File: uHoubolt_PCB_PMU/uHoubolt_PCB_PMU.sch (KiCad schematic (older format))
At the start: 44 parts, among them J1 Conn_01x04, J2 Conn_01x02, J3 Conn_01x04, Q1 ZXMN3F30FH, Q2 Si7141DP, SW1 SW_Push_SPDT, SW2 SW_Push_SPDT, U1 INA226, U2 MAX1873SEEE

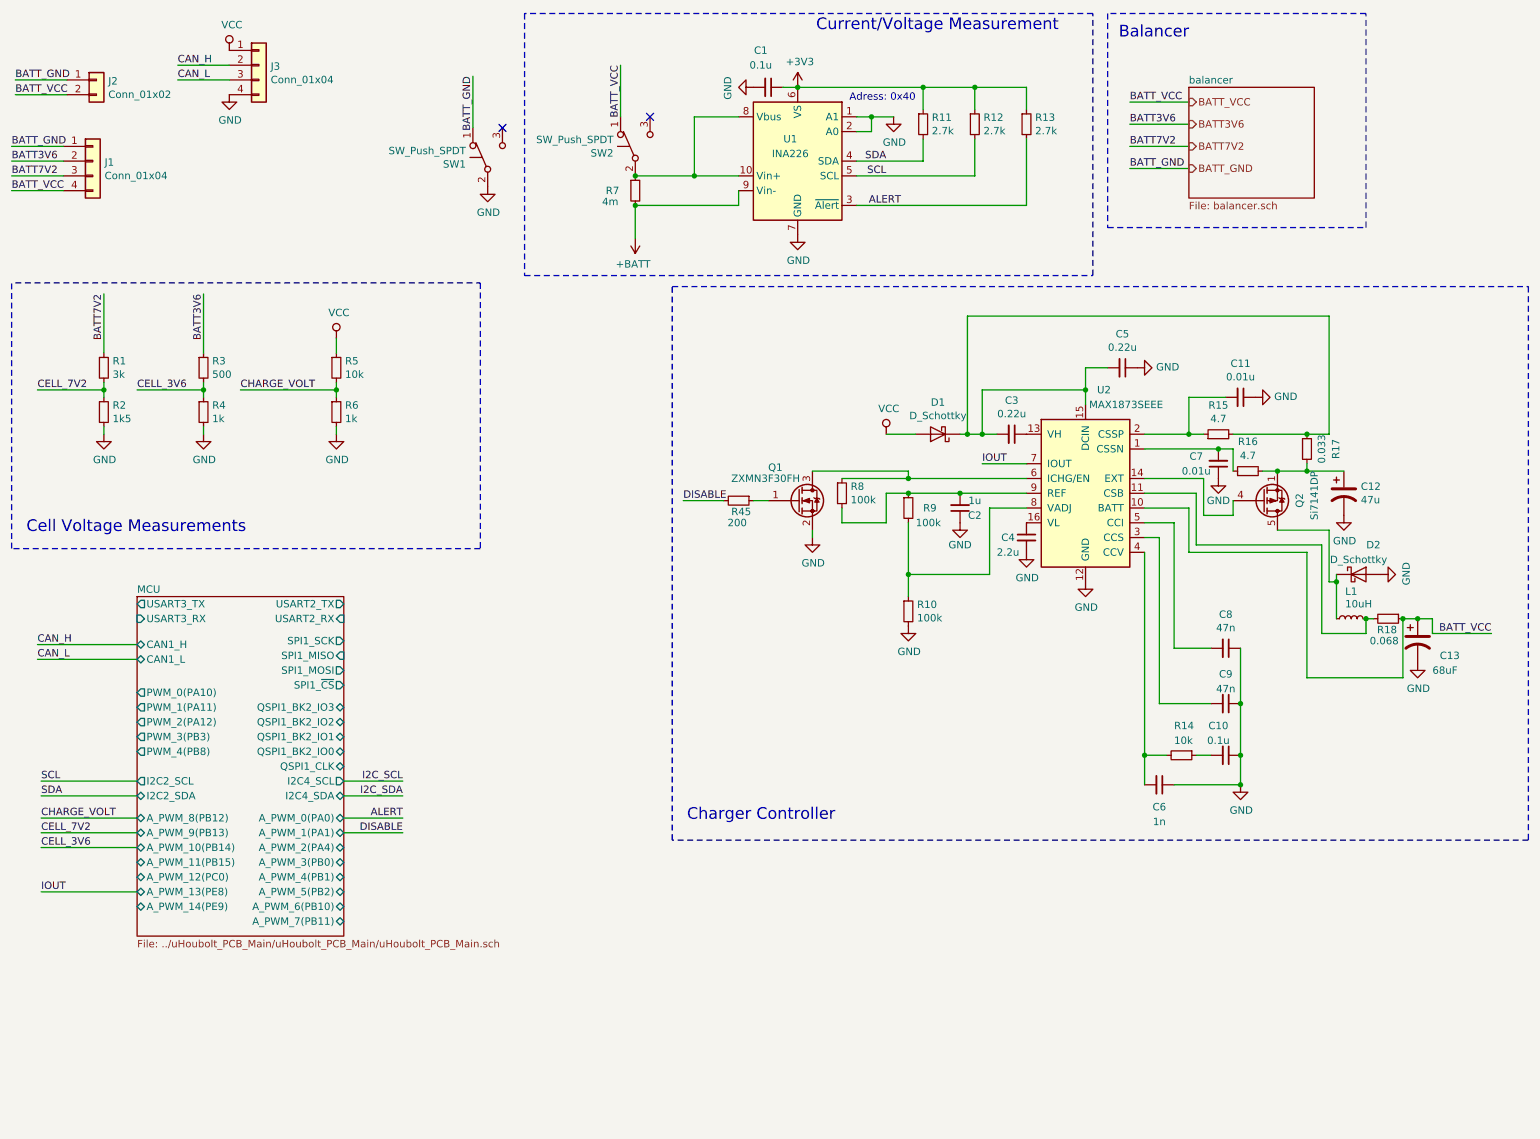
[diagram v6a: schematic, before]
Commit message: unify notation, connect NoConnects, revise balancer, add output connector
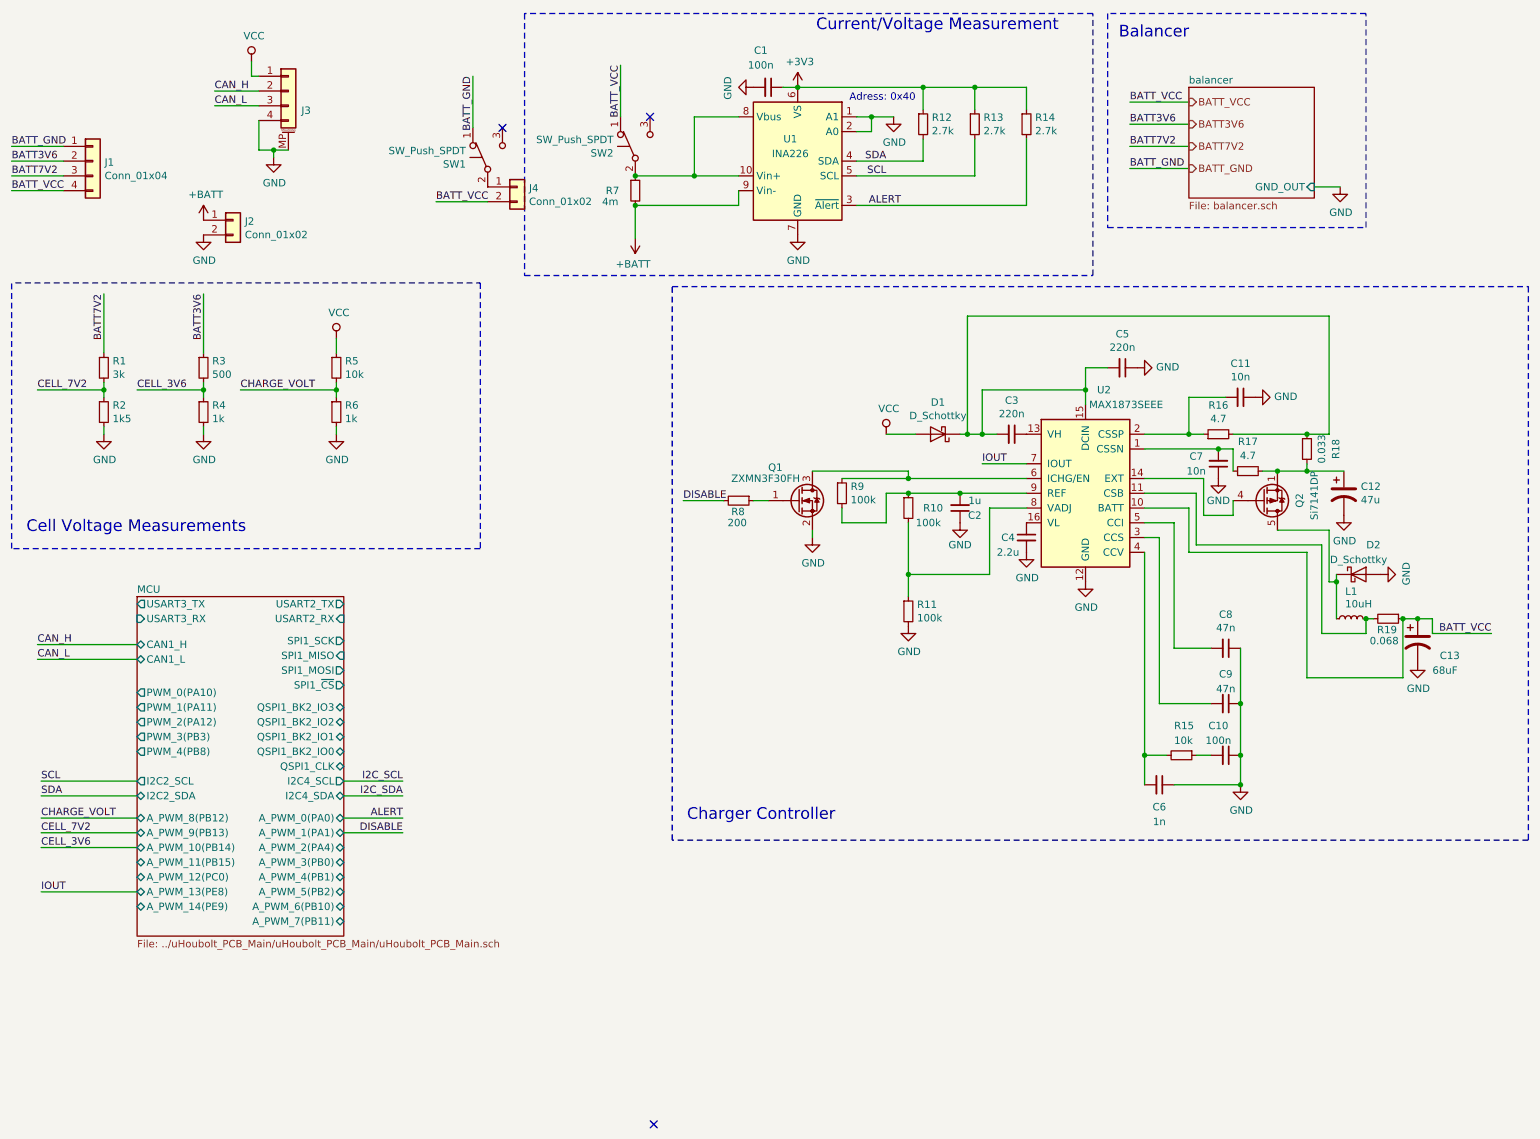
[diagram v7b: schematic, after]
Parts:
- removed J3: Conn_01x04, symbol Connector_Generic:Conn_01x04
- added J2: Conn_01x02, symbol Connector_Generic:Conn_01x02
- added J3: Conn_01x04_MountingPin, symbol Connector_Generic_MountingPin:Conn_01x04_MountingPin
- C1, C10: value 0.1u -> 100n
- C11, C7: value 0.01u -> 10n
- C3, C5: value 0.22u -> 220n
- renumbered J2 to J4, R9 to R10, R10 to R11, R11 to R12, R12 to R13, R13 to R14, R14 to R15, R15 to R16, R16 to R17, R17 to R18, R18 to R19, R45 to R8, R8 to R9
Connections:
- net +BATT: now also J2.1 (Pin_1)
- net BATT_GND: no longer J4.1 (Pin_1)
- net CAN_H: now also J3.2 (Pin_2)
- net CAN_L: now also J3.3 (Pin_3)
- net GND: now also J2.2 (Pin_2), J3.4 (Pin_4), J3.MP (MountPin); no longer SW1.2 (B)
- net VCC: now also J3.1 (Pin_1)
- new net: J4.1 (Pin_1), SW1.2 (B)
- no-connect marks 2 -> 3
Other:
- moved on the sheet: J4

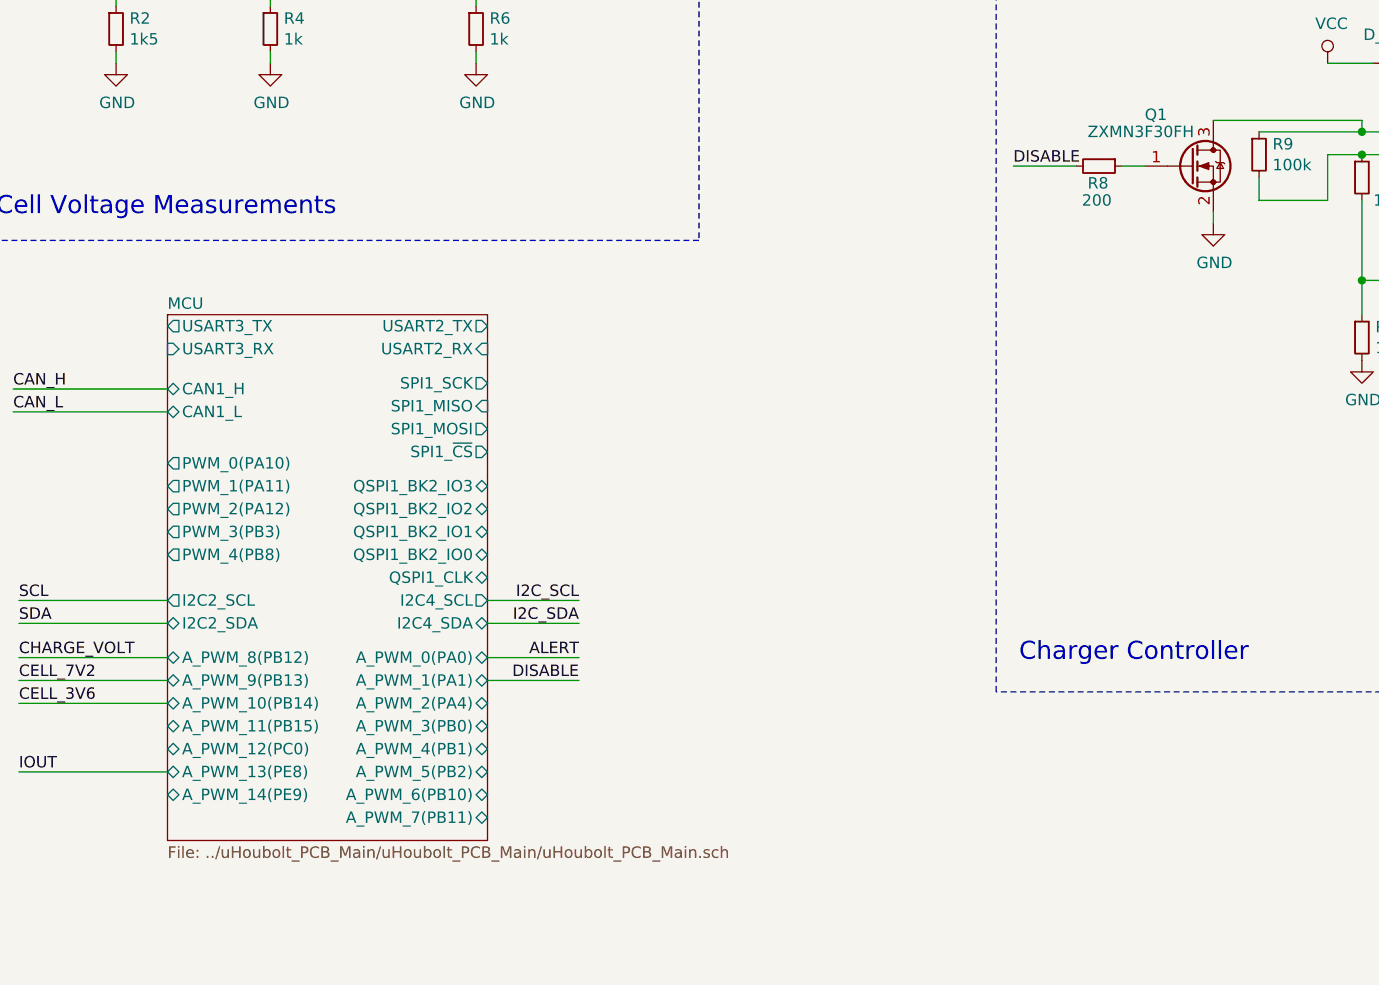
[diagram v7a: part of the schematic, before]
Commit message: add NoConnects, add capacitor footprints, add pulldown to Q1
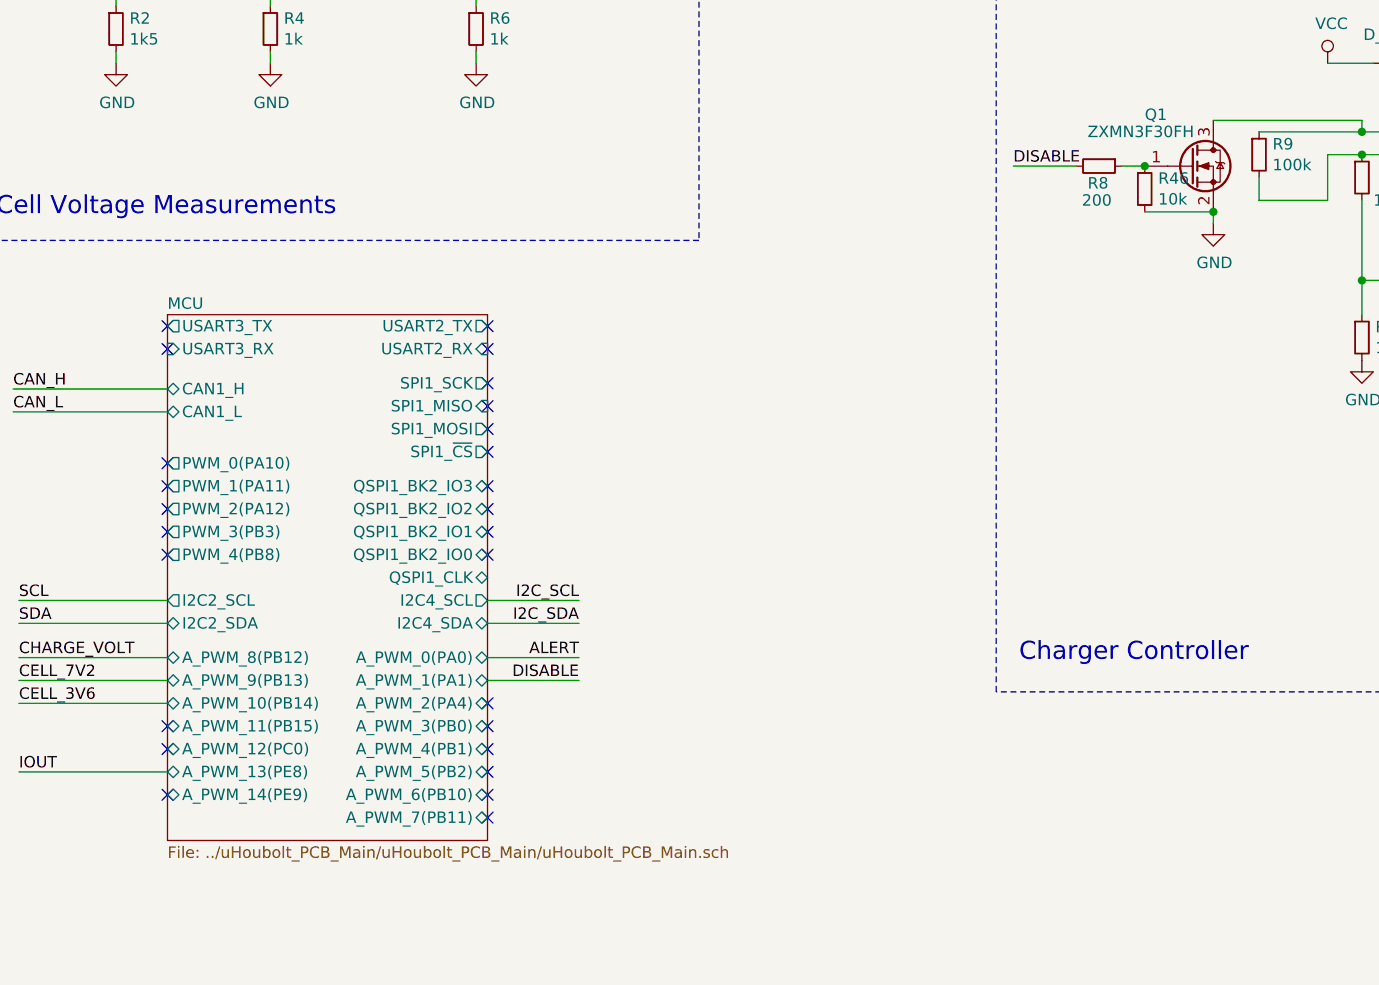
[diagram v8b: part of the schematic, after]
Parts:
- added R46: 10k, symbol Device:R_Small
- C1, C10, C11, C3, C5, C6, C7, C8, C9: footprint (none) -> Capacitor_SMD:C_0402_1005Metric
- C2, C4: footprint (none) -> Capacitor_SMD:C_0603_1608Metric
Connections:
- net GND: now also R46.2
- net at Q1.1 (G), R8.1: now also R46.1
- no-connect marks 3 -> 29
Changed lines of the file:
@@
 F 0 "C5" V 7921 2950 50  0000 C CNN
 F 1 "220n" V 8012 2950 50  0000 C CNN
-F 2 "" H 8150 2950 50  0001 C CNN
+F 2 "Capacitor_SMD:C_0402_1005Metric" H 8150 2950 50  0001 C CNN
 F 3 "~" H 8150 2950 50  0001 C CNN
 	1    8150 2950
@@
 F 0 "C11" V 8721 3150 50  0000 C CNN
 F 1 "10n" V 8812 3150 50  0000 C CNN
-F 2 "" H 8950 3150 50  0001 C CNN
+F 2 "Capacitor_SMD:C_0402_1005Metric" H 8950 3150 50  0001 C CNN
 F 3 "~" H 8950 3150 50  0001 C CNN
 	1    8950 3150
@@
 F 0 "C3" V 7171 3400 50  0000 C CNN
 F 1 "220n" V 7262 3400 50  0000 C CNN
-F 2 "" H 7400 3400 50  0001 C CNN
+F 2 "Capacitor_SMD:C_0402_1005Metric" H 7400 3400 50  0001 C CNN
 F 3 "~" H 7400 3400 50  0001 C CNN
 	1    7400 3400
@@
 F 0 "C2" H 6950 3950 50  0000 C CNN
 F 1 "1u" H 6950 3850 50  0000 C CNN
-F 2 "" H 7050 3900 50  0001 C CNN
+F 2 "Capacitor_SMD:C_0603_1608Metric" H 7050 3900 50  0001 C CNN
 F 3 "~" H 7050 3900 50  0001 C CNN
 	1    7050 3900
@@
 F 0 "C8" V 8621 4850 50  0000 C CNN
 F 1 "47n" V 8712 4850 50  0000 C CNN
-F 2 "" H 8850 4850 50  0001 C CNN
+F 2 "Capacitor_SMD:C_0402_1005Metric" H 8850 4850 50  0001 C CNN
 F 3 "~" H 8850 4850 50  0001 C CNN
 	1    8850 4850
@@
 F 0 "C9" V 8650 5225 50  0000 C CNN
 F 1 "47n" V 8750 5225 50  0000 C CNN
-F 2 "" H 8850 5225 50  0001 C CNN
+F 2 "Capacitor_SMD:C_0402_1005Metric" H 8850 5225 50  0001 C CNN
 F 3 "~" H 8850 5225 50  0001 C CNN
 	1    8850 5225
@@
 F 0 "C10" V 8650 5525 50  0000 C CNN
 F 1 "100n" V 8750 5525 50  0000 C CNN
-F 2 "" H 8850 5575 50  0001 C CNN
+F 2 "Capacitor_SMD:C_0402_1005Metric" H 8850 5575 50  0001 C CNN
 F 3 "~" H 8850 5575 50  0001 C CNN
 	1    8850 5575
@@
 F 0 "C6" V 8550 5775 50  0000 C CNN
 F 1 "1n" V 8650 5775 50  0000 C CNN
-F 2 "" H 8400 5775 50  0001 C CNN
+F 2 "Capacitor_SMD:C_0402_1005Metric" H 8400 5775 50  0001 C CNN
 F 3 "~" H 8400 5775 50  0001 C CNN
 	1    8400 5775
@@
 F 0 "C4" H 7375 4100 50  0000 C CNN
 F 1 "2.2u" H 7375 4000 50  0000 C CNN
-F 2 "" H 7500 4100 50  0001 C CNN
+F 2 "Capacitor_SMD:C_0603_1608Metric" H 7500 4100 50  0001 C CNN
 F 3 "~" H 7500 4100 50  0001 C CNN
 	1    7500 4100
@@
 F 0 "C7" H 8950 3550 50  0000 C CNN
 F 1 "10n" H 8950 3650 50  0000 C CNN
-F 2 "" H 8800 3600 50  0001 C CNN
+F 2 "Capacitor_SMD:C_0402_1005Metric" H 8800 3600 50  0001 C CNN
 F 3 "~" H 8800 3600 50  0001 C CNN
 	1    8800 3600
@@
 F 0 "C1" V 5500 1000 50  0000 C CNN
 F 1 "100n" V 5600 1000 50  0000 C CNN
-F 2 "" H 5750 1050 50  0001 C CNN
+F 2 "Capacitor_SMD:C_0402_1005Metric" H 5750 1050 50  0001 C CNN
 F 3 "~" H 5750 1050 50  0001 C CNN
 	1    5750 1050
@@
 	9450 1725 9625 1725
 NoConn ~ 4975 8075
+NoConn ~ 1475 5150
+NoConn ~ 1475 5350
+NoConn ~ 1475 5450
+NoConn ~ 1475 5550
+NoConn ~ 2875 4550
+NoConn ~ 1475 4650
+NoConn ~ 2875 4650
+NoConn ~ 2875 4800
+NoConn ~ 1475 5250
+NoConn ~ 1475 4550
+NoConn ~ 1475 6300
+NoConn ~ 1475 6400
+NoConn ~ 1475 6600
+NoConn ~ 2875 4900
+NoConn ~ 2875 5000
+NoConn ~ 2875 5100
+NoConn ~ 2875 5250
+NoConn ~ 2875 5350
+NoConn ~ 2875 5450
+NoConn ~ 2875 5550
+NoConn ~ 2875 6200
+NoConn ~ 2875 6300
+NoConn ~ 2875 6400
+NoConn ~ 2875 6500
+NoConn ~ 2875 6600
+NoConn ~ 2875 6700
+$Comp
+L Device:R_Small R46
+U 1 1 60205DC9
+P 5750 3950
+F 0 "R46" H 5809 3996 50  0000 L CNN
+F 1 "10k" H 5809 3905 50  0000 L CNN
+F 2 "" H 5750 3950 50  0001 C CNN
+F 3 "~" H 5750 3950 50  0001 C CNN
+	1    5750 3950
+	1    0    0    -1
+$EndComp
+Connection ~ 5750 3850
+Wire Wire Line
+	5750 4050 6050 4050
+Connection ~ 6050 4050
 $EndSCHEMATC
